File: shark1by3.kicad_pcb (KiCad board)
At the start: 2 copper layers, 57.2 x 46 mm, 26 parts, among them SW1 SW_Push_Reset, U1 PRTR5V0U2X, U2 ATmega32U4-A, X1 16MHz

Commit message: antishear bois
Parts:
- MX1, MX2, MX3: footprint MX_Only:MXOnly-1U-Hotswap -> MX_Only:MXOnly-1U-Hotswap-Antishear
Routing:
- net col0: track 28.5 -> 26.4 mm
- net col2: track 47.1 -> 45.5 mm, vias 4 -> 3
- net Net-(MX2-Pad2): track 9.06 -> 7.96 mm
- net col1: track 30.1 -> 29.4 mm

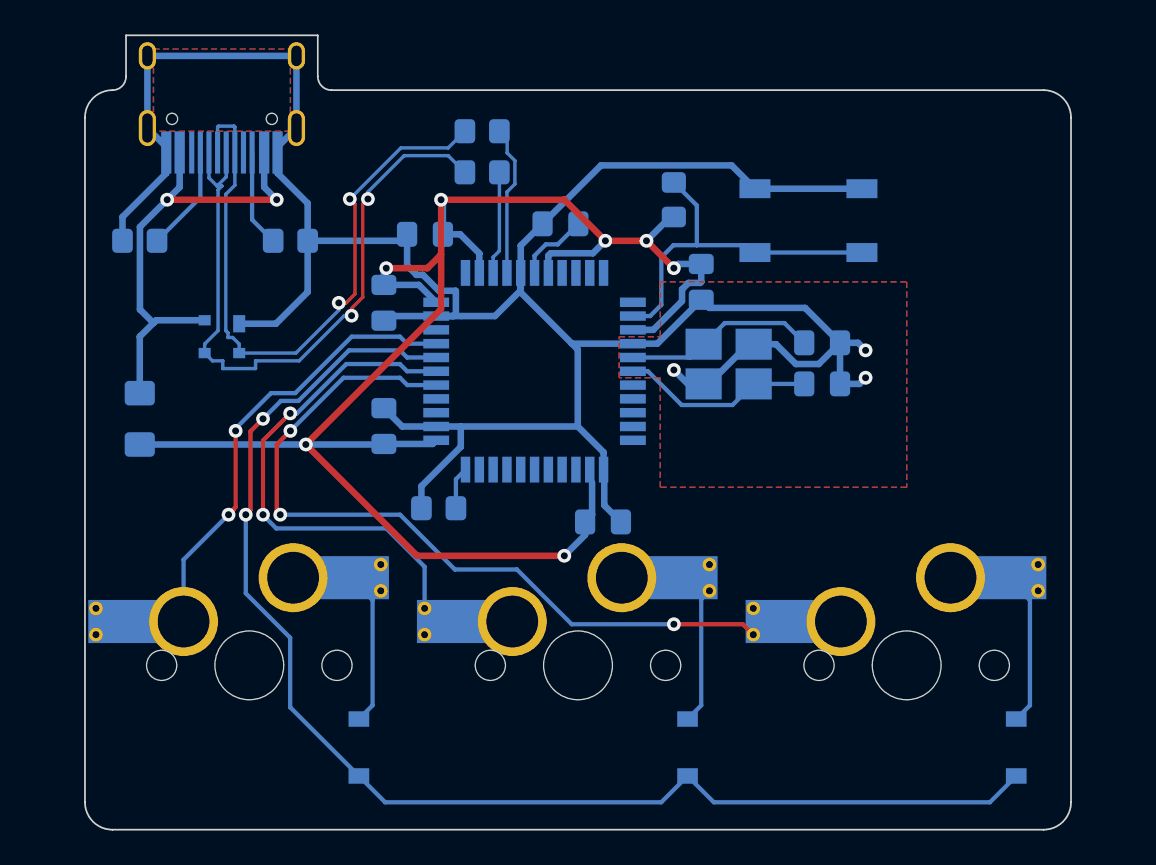
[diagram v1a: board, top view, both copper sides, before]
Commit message: add silk screen stuff
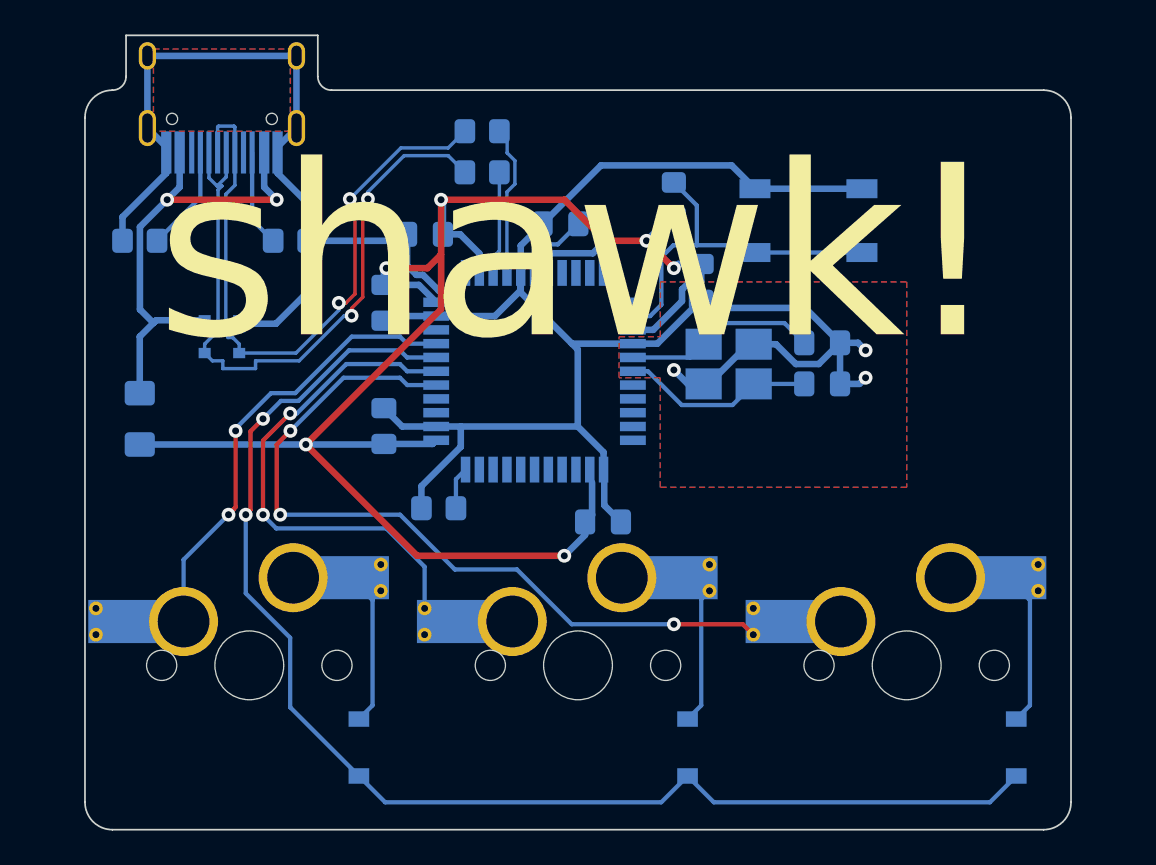
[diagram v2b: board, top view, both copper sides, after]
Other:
- board text added: "shark! v1.0"
- board text added: "shawk!"
